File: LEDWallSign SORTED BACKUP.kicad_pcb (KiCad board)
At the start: 2 copper layers, 207 parts, among them J1 ISP Header, P1 Conn_WallPlug, SW1 KSR251GLFS, U1 ATmega328-AU, U100 TLC6C598-Q1, U2 RAC10-05SK, U200 TLC6C598-Q1, U300 TLC6C598-Q1, U400 TLC6C598-Q1, U500 TLC6C598-Q1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

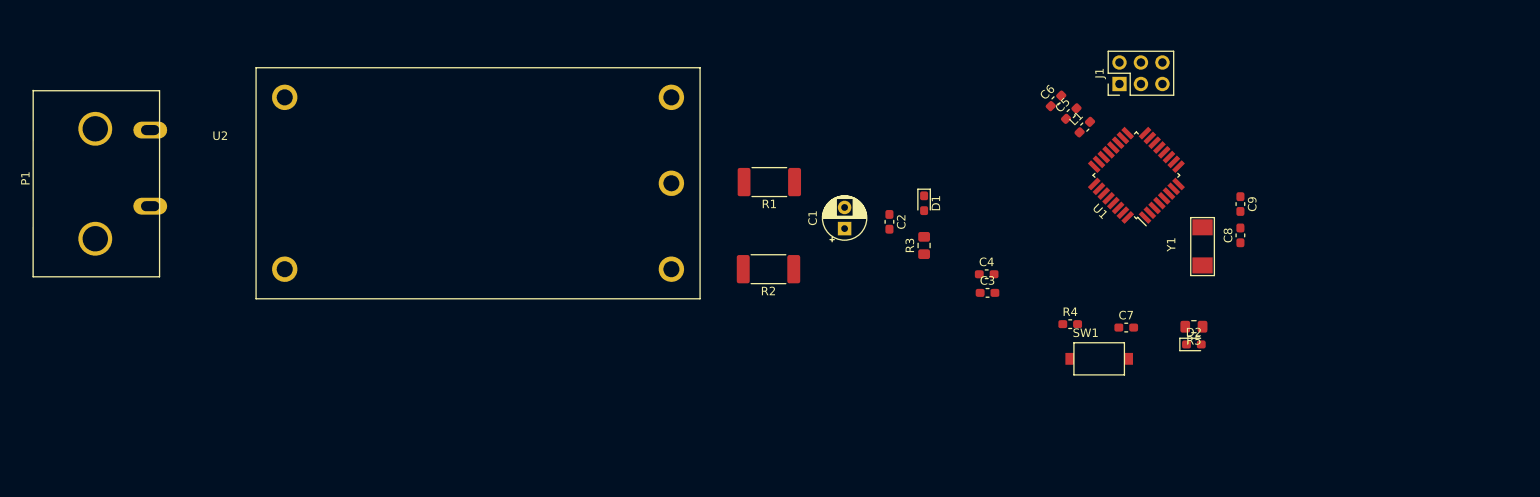
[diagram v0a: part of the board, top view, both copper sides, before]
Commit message: References and footprints completed. Added back up layout (of components sorted)
Going to play around with the layout now. Eventually hope to get final one done by end of this week.
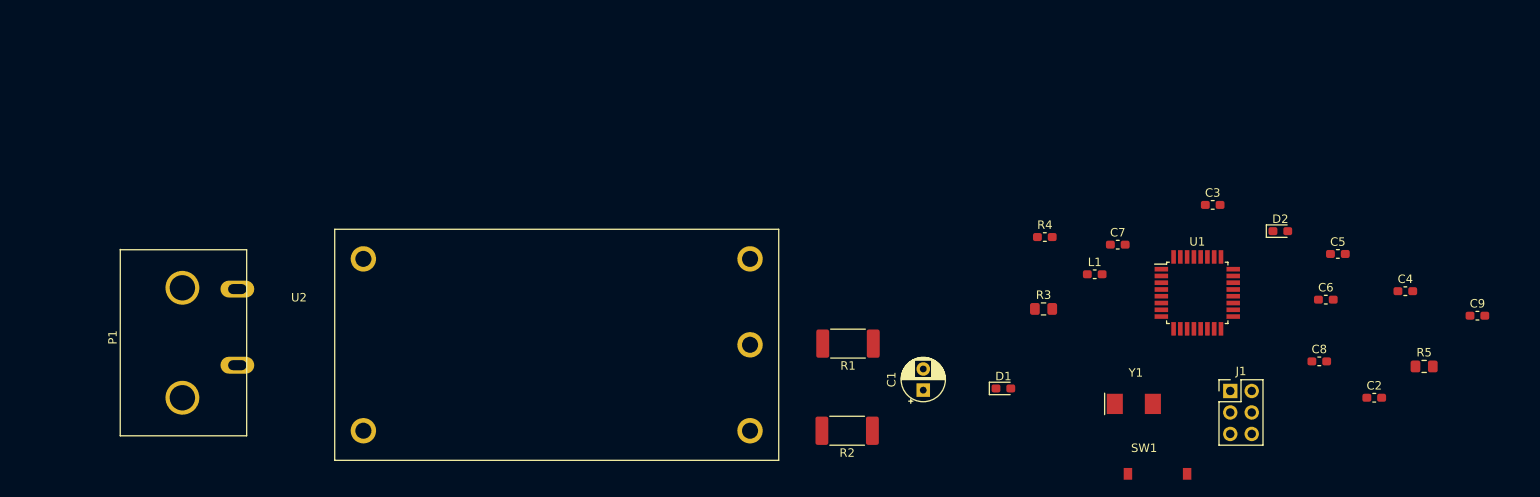
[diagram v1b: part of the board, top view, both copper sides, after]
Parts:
- moved C2 61.0 mm to (181.5, 161.0), turned to 0 degrees
- moved C4 49.5 mm to (185.2, 148.4)
- moved C6 39.6 mm to (175.8, 149.4), turned to 0 degrees
- moved J1 38.6 mm to (164.5, 160.2), turned to 0 degrees
- moved C5 35.6 mm to (177.2, 144.0), turned to 0 degrees
- moved C9 31.0 mm to (193.7, 151.3), turned to 0 degrees
- moved C3 28.6 mm to (162.4, 138.2)
- moved R5 27.6 mm to (187.4, 157.3), turned to 0 degrees
- moved D1 23.8 mm to (137.7, 159.9), turned to 0 degrees
- moved P1 21.4 mm to (47.1, 154.5)
- moved R1 21.2 mm to (119.3, 154.6)
- moved R2 21.2 mm to (119.2, 164.9)
- moved U2 21.2 mm to (62.0, 164.9)
- moved C1 21.2 mm to (128.2, 160.1)
- moved Y1 19.0 mm to (149.9, 161.6), turned to 0 degrees
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
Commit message: Fully organized parts into their subsystem categories. Also added new backup file for layout.
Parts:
- moved R749 230.5 mm to (42.9, 127.9)
- moved R750 221.6 mm to (50.5, 128.0)
- moved R640 218.2 mm to (50.6, 112.6)
- moved D641 211.0 mm to (56.1, 112.1)
- moved D750 210.1 mm to (50.0, 125.6)
- moved R641 206.1 mm to (56.5, 110.1)
- moved D752 201.0 mm to (67.2, 128.7)
- moved D857 201.0 mm to (52.8, 143.5)
- moved R752 197.8 mm to (67.7, 126.0)
- moved D642 194.5 mm to (61.4, 111.8)
- moved D749 192.3 mm to (43.1, 125.6)
- moved D856 192.2 mm to (47.2, 143.5)
- moved R644 191.7 mm to (72.3, 112.5)
- moved R754 190.4 mm to (83.7, 129.2)
- moved D645 190.3 mm to (78.4, 113.5)
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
